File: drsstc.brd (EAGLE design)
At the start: 99.1 x 99.1 mm, 125 parts, among them U1 AP1501, U10 LM311, U11 74HC74, U12 LM8365, U13 ICM7216D, U14 ICM7216D, U2 74AHCT1G32, U3 AP1506, U4 MCP4706, U5 UCC27423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

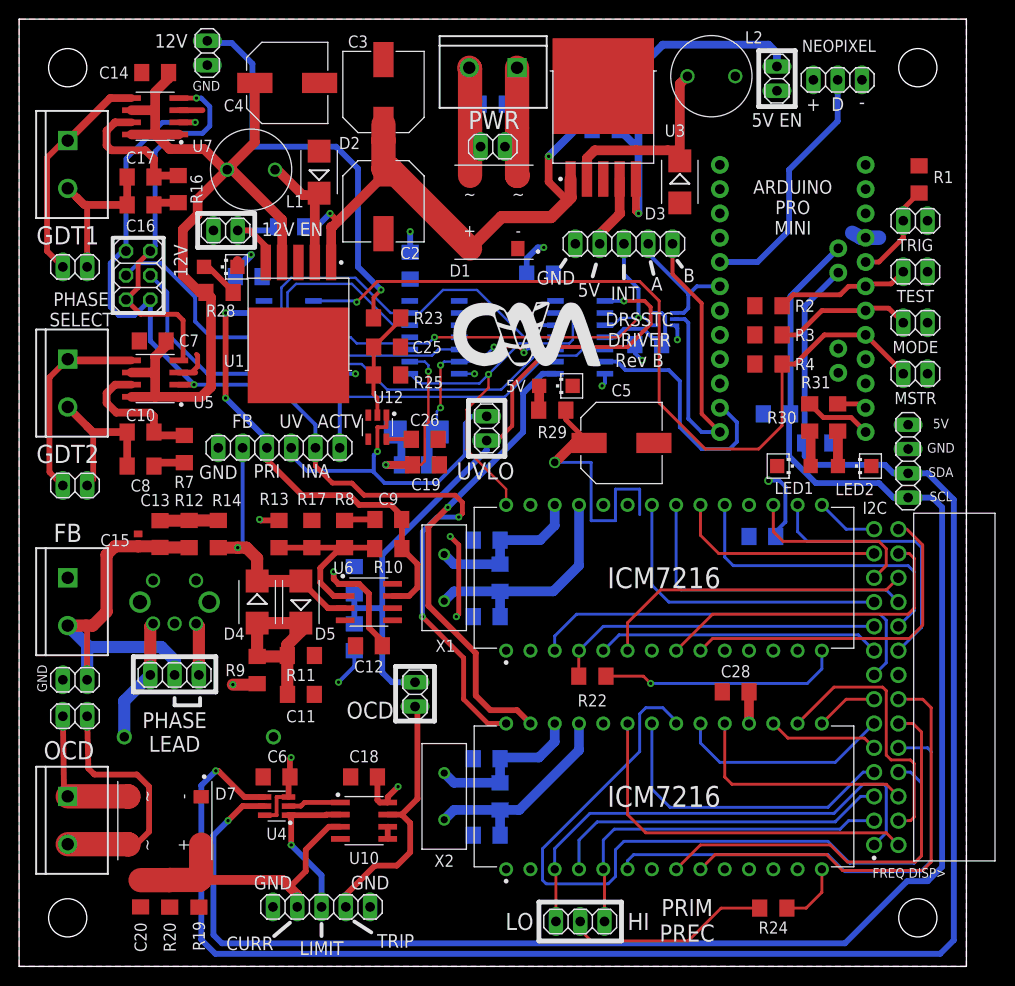
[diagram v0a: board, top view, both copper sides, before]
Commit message: Updating Rev B board with hysteresis feedback fix
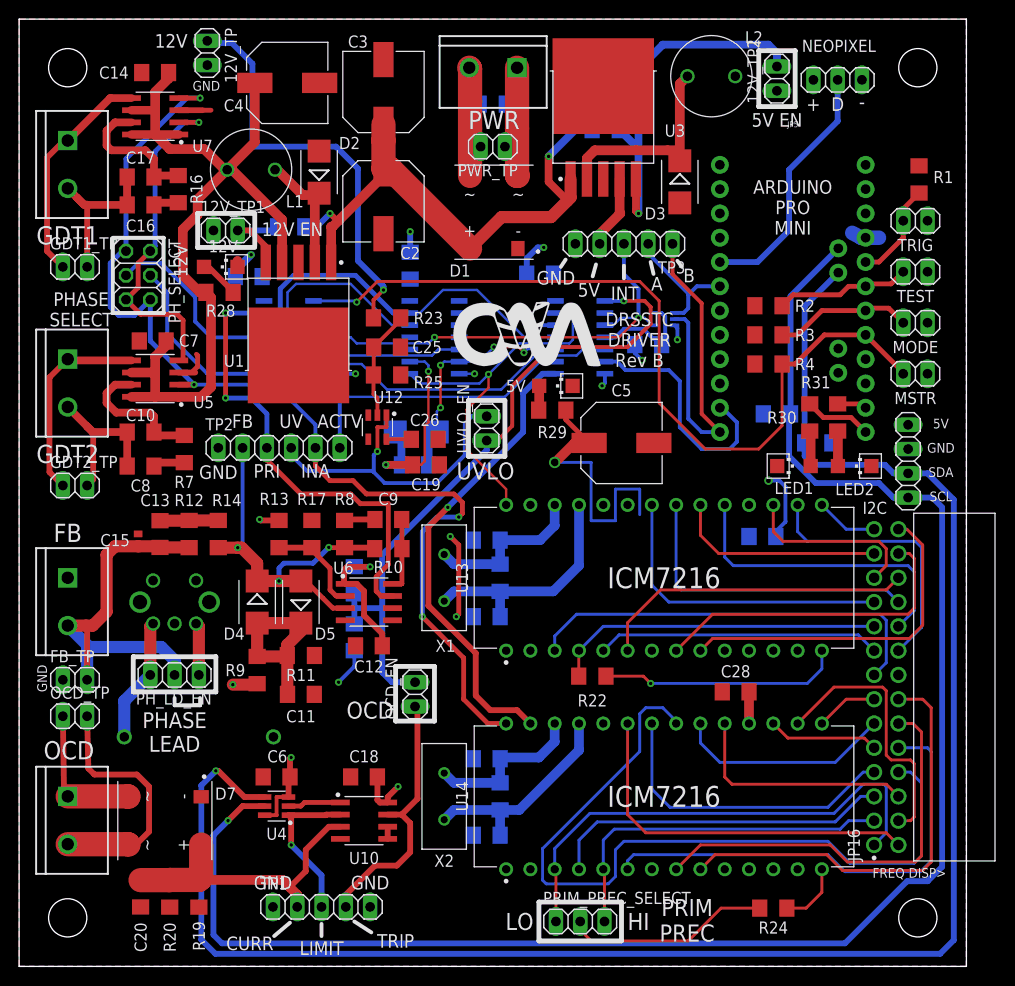
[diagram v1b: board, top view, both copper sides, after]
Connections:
- new net N$26: R13.1, R17.2, U6.2
- net FB_IN: now also R10.2, R8.2
- net INA: now also U7.4; no longer U7.2
- net INB: now also U7.2; no longer U7.4
- net N$23: now also C9.2, R10.1, U6.8; no longer R10.2, R13.1, R17.2, R8.2, U6.2
- net PRIMARY: no longer C9.2, R10.1
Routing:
- net FB_IN: track 27.9 -> 40.4 mm, vias 1 -> 3
- net N$26: track 0.00 -> 10.5 mm
- net N$23: track 18.2 -> 7.71 mm
- net INB: track 40.7 -> 36.2 mm
- net INA: track 111.2 -> 113.3 mm
- net VCC: track 94.0 -> 96.0 mm
- net GND: track 49.4 -> 50.3 mm
